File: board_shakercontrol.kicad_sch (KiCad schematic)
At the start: 20 parts, among them J1 Power, J2 Power, J3 Conn_01x04_Male, J4 SHAKER, Q1 IRF640NS, U1 L7805, U2 LTV-817

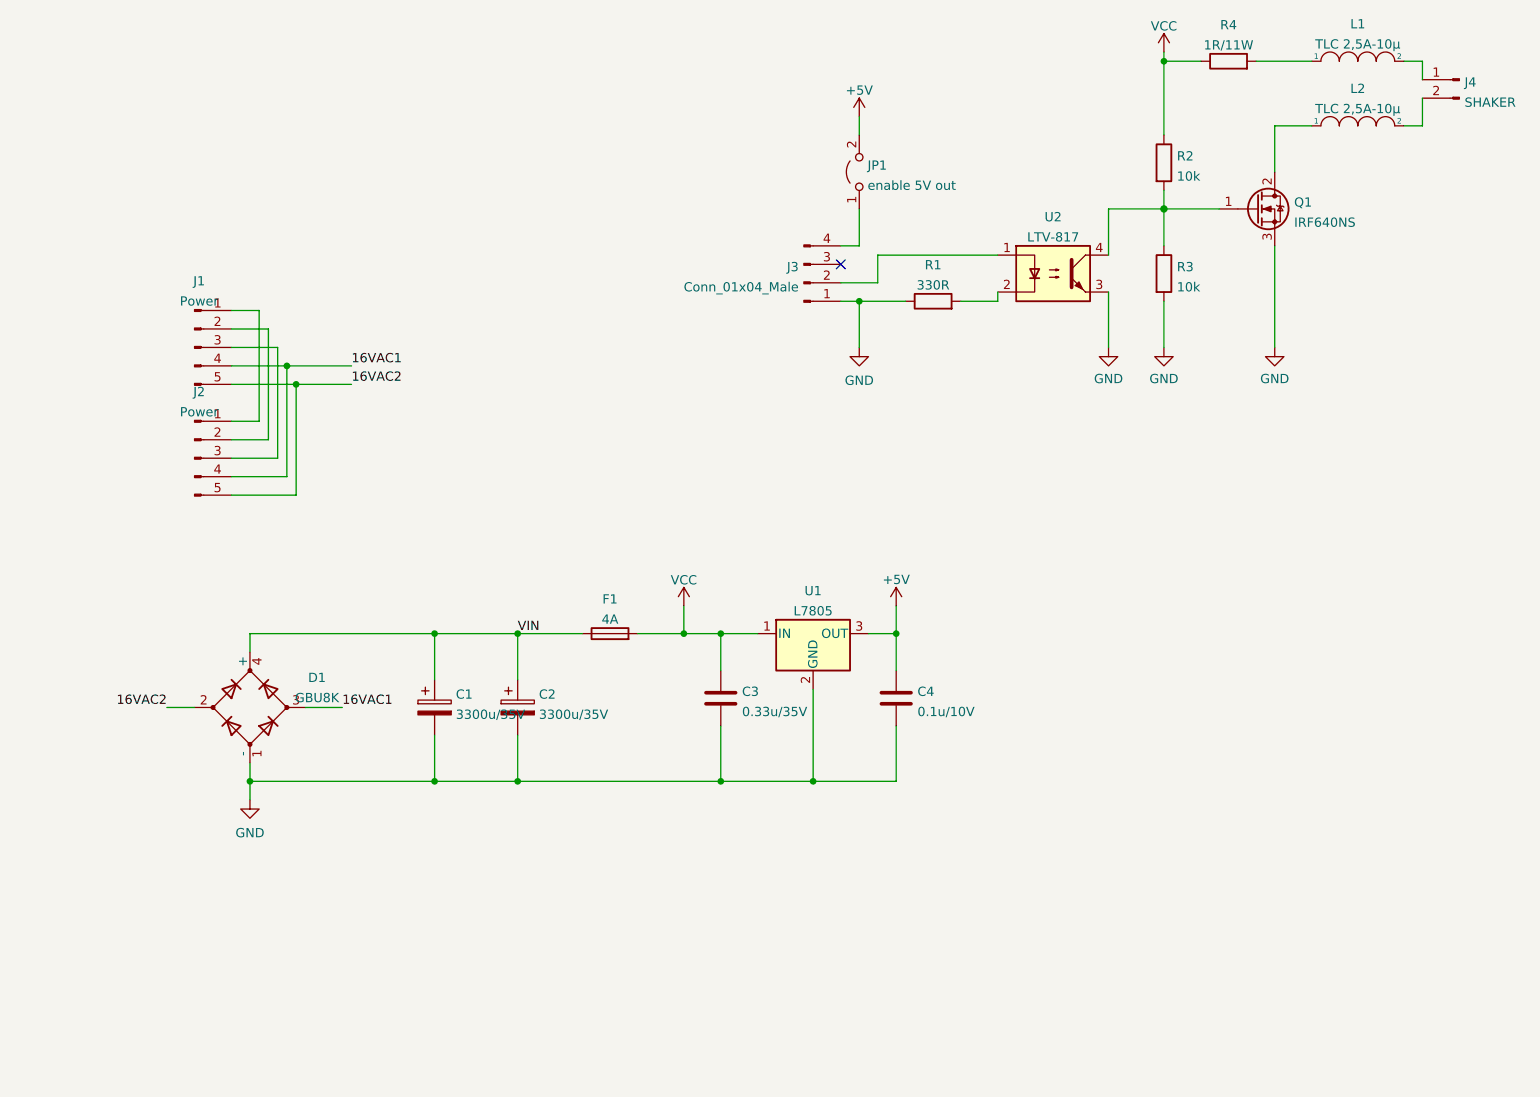
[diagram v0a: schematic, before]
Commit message: Changed control connection from 4 to 3 pin
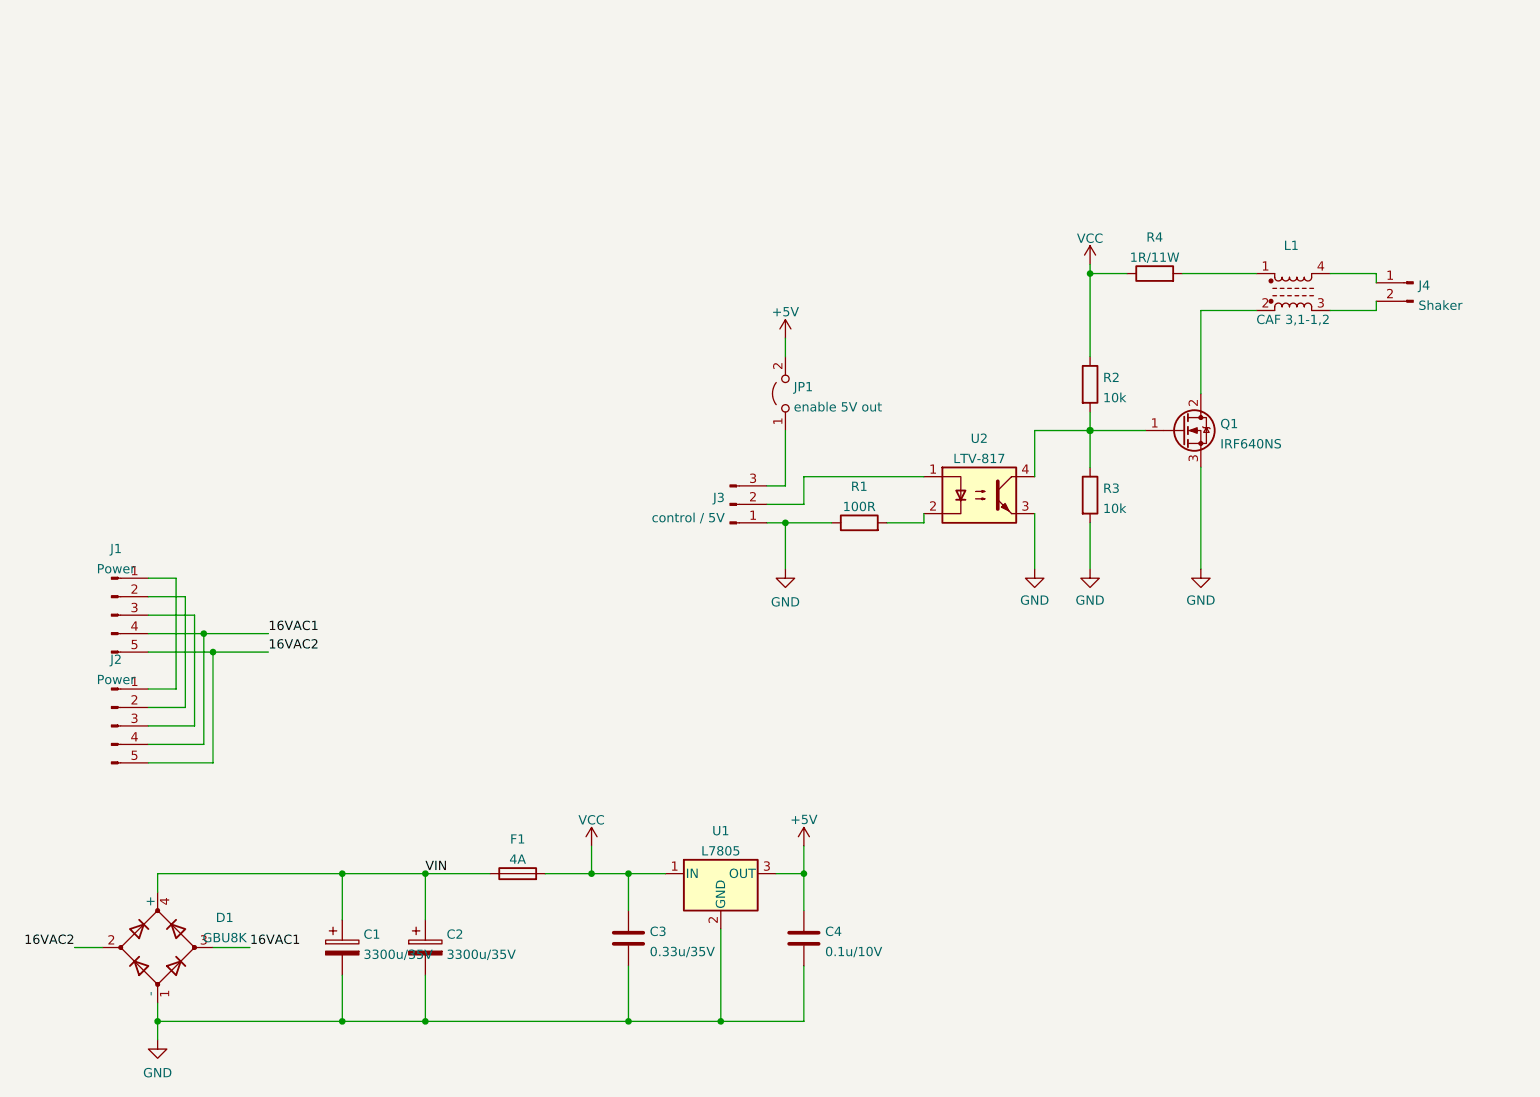
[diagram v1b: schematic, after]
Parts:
- removed J3: Conn_01x04_Male, Connector_Molex:Molex_KK-254_AE-6410-04A_1x04_P2.54mm_Vertical, symbol Connector:Conn_01x04_Male
- removed L1, L2: TLC 2,5A-10µ, Inductor_THT:L_Toroid_Vertical_L19.1mm_W8.1mm_P7.10mm_Bourns_5700, symbol pspice:INDUCTOR
- added J3: control / 5V, Connector_Molex:Molex_KK-254_AE-6410-03A_1x03_P2.54mm_Vertical, symbol Connector:Conn_01x03_Male
- added L1: CAF 3,1-1,2, cmchoke:CAF-12.5x20, symbol Device:L_Ferrite_Coupled_1423
- J4: value SHAKER -> Shaker
- R1: value 330R -> 100R
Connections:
- net GND: now also J3.1 (Pin_1)
- net at R4.2: now also L1.1
- net at JP1.1 (A): now also J3.3 (Pin_3)
- net at Q1.2 (D): now also L1.2
- net at J4.2 (Pin_2): now also L1.3
- net at J4.1 (Pin_1): now also L1.4
- net at U2.1: now also J3.2 (Pin_2)
- no-connect marks 1 -> 0
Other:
- moved on the sheet: C1, C2, C3, C4, D1, F1, J1, J2, J4, JP1, Q1, R1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
